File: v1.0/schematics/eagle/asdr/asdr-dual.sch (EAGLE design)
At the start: 56 parts, among them IC3 NE556, IC4 TL082P, Q1 2N3417, Q2 2N3417, Q3 2N3417, Q4 2N3417, Q5 2N3417, Q6 2N3417

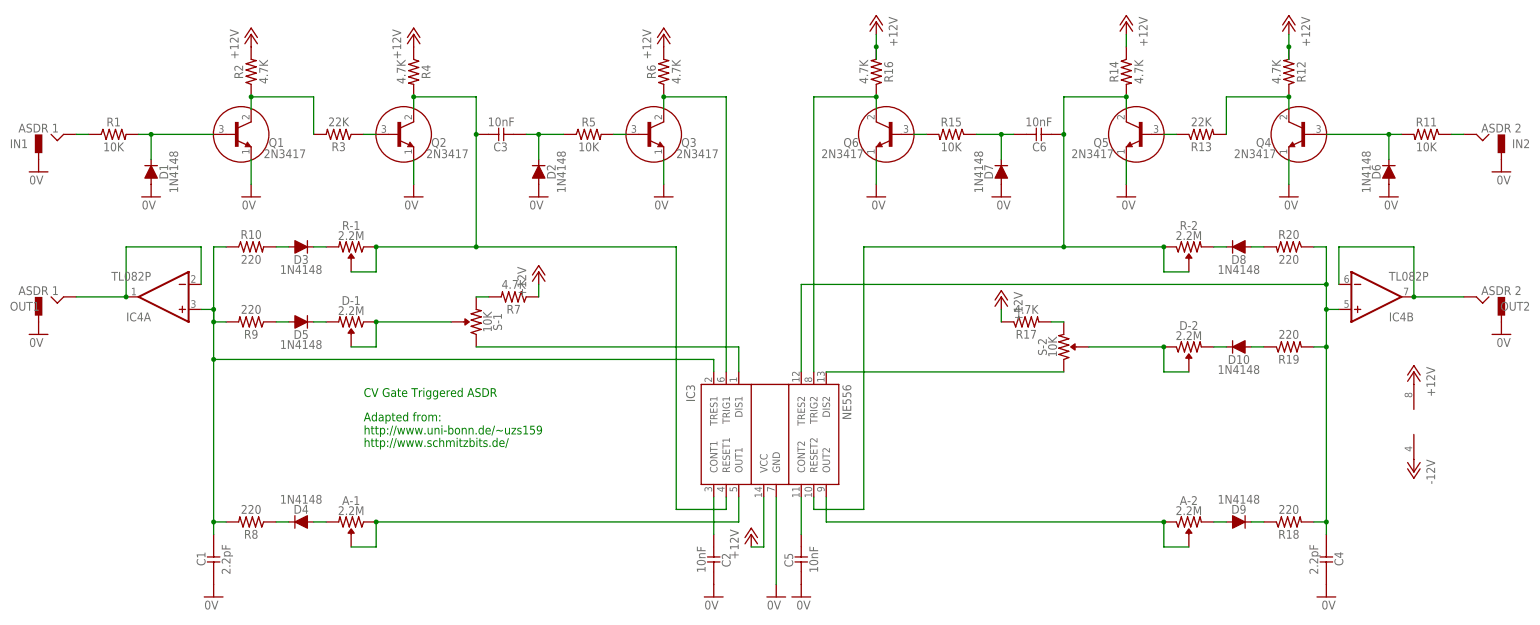
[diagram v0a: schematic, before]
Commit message: Updated ASDR with revised values
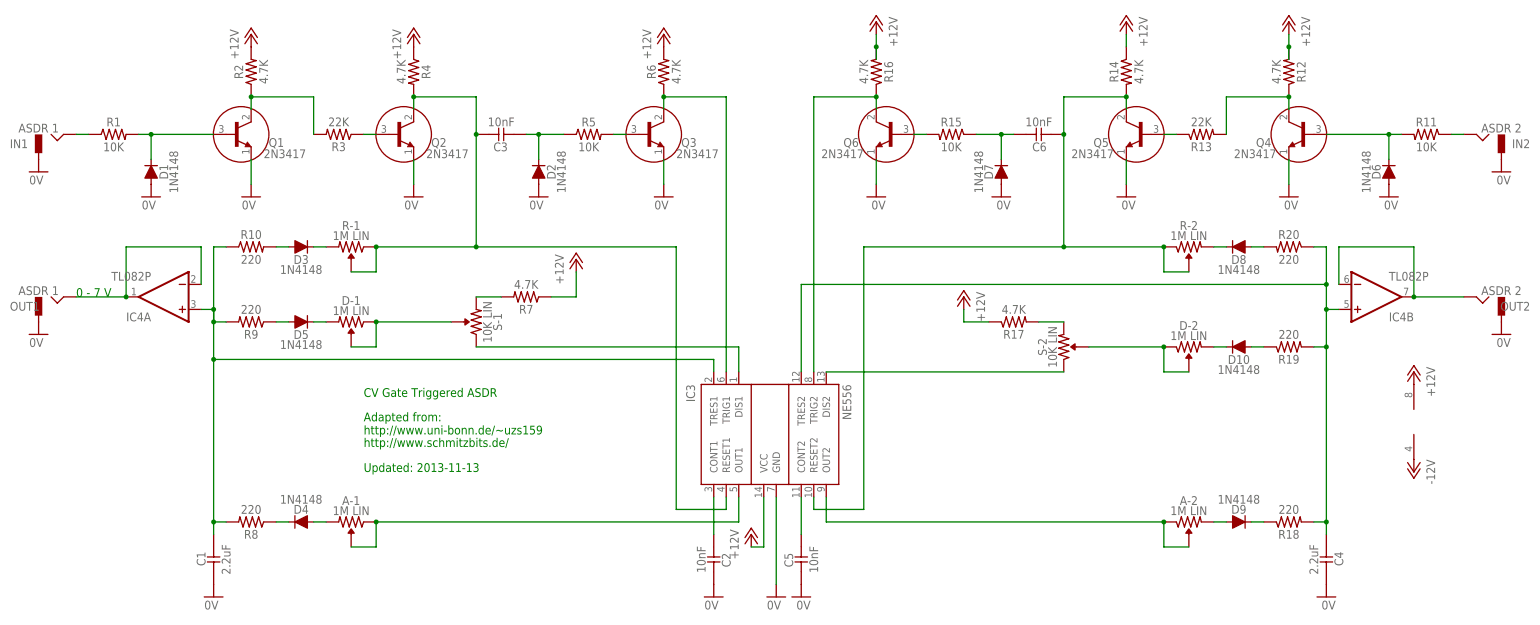
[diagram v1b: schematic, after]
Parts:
- A-1, A-2, D-1, D-2, R-1, R-2: value 2.2M -> 1M LIN
- C1, C4: value 2.2pF -> 2.2uF
- S-1, S-2: value 10K -> 10K LIN
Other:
- note added: "0 - 7 V"
- note added: "Updated: 2013-11-13"
- moved on the sheet: R17, R7
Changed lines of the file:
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@@
 <part name="R6" library="_common" deviceset="R" device="0309/10" value="4.7K"/>
 <part name="R7" library="_common" deviceset="R" device="0309/10" value="4.7K"/>
-<part name="S-1" library="_common" deviceset="R-VAR" device="" value="10K"/>
-<part name="D-1" library="_common" deviceset="R-VAR" device="" value="2.2M"/>
-<part name="A-1" library="_common" deviceset="R-VAR" device="" value="2.2M"/>
-<part name="R-1" library="_common" deviceset="R-VAR" device="" value="2.2M"/>
+<part name="S-1" library="_common" deviceset="R-VAR" device="" value="10K LIN"/>
+<part name="D-1" library="_common" deviceset="R-VAR" device="" value="1M LIN"/>
+<part name="A-1" library="_common" deviceset="R-VAR" device="" value="1M LIN"/>
+<part name="R-1" library="_common" deviceset="R-VAR" device="" value="1M LIN"/>
 <part name="R8" library="_common" deviceset="R" device="0309/10" value="220"/>
 <part name="R9" library="_common" deviceset="R" device="0309/10" value="220"/>
@@
 <part name="D5" library="_common" deviceset="1N4148" device=""/>
 <part name="R10" library="_common" deviceset="R" device="0309/10" value="220"/>
-<part name="C1" library="_common" deviceset="CC-US" device="025-024X044" value="2.2pF"/>
+<part name="C1" library="_common" deviceset="CC-US" device="025-024X044" value="2.2uF"/>
 <part name="C2" library="_common" deviceset="CC-US" device="025-024X044" value="10nF"/>
 <part name="C3" library="_common" deviceset="CC-US" device="025-024X044" value="10nF"/>
@@
 <part name="R16" library="_common" deviceset="R" device="0309/10" value="4.7K"/>
 <part name="R17" library="_common" deviceset="R" device="0309/10" value="4.7K"/>
-<part name="S-2" library="_common" deviceset="R-VAR" device="" value="10K"/>
-<part name="D-2" library="_common" deviceset="R-VAR" device="" value="2.2M"/>
-<part name="A-2" library="_common" deviceset="R-VAR" device="" value="2.2M"/>
-<part name="R-2" library="_common" deviceset="R-VAR" device="" value="2.2M"/>
+<part name="S-2" library="_common" deviceset="R-VAR" device="" value="10K LIN"/>
+<part name="D-2" library="_common" deviceset="R-VAR" device="" value="1M LIN"/>
+<part name="A-2" library="_common" deviceset="R-VAR" device="" value="1M LIN"/>
+<part name="R-2" library="_common" deviceset="R-VAR" device="" value="1M LIN"/>
 <part name="R18" library="_common" deviceset="R" device="0309/10" value="220"/>
 <part name="R19" library="_common" deviceset="R" device="0309/10" value="220"/>
@@
 <part name="D10" library="_common" deviceset="1N4148" device=""/>
 <part name="R20" library="_common" deviceset="R" device="0309/10" value="220"/>
-<part name="C4" library="_common" deviceset="CC-US" device="025-024X044" value="2.2pF"/>
+<part name="C4" library="_common" deviceset="CC-US" device="025-024X044" value="2.2uF"/>
 <part name="C5" library="_common" deviceset="CC-US" device="025-024X044" value="10nF"/>
 <part name="C6" library="_common" deviceset="CC-US" device="025-024X044" value="10nF"/>
@@
 http://www.uni-bonn.de/~uzs159</text>
 <text x="50.8" y="20.32" size="1.778" layer="91">http://www.schmitzbits.de/</text>
+<text x="50.8" y="15.24" size="1.778" layer="91">Updated: 2013-11-13</text>
+<text x="-7.62" y="50.8" size="1.778" layer="91">0 - 7 V</text>
 </plain>
 <instances>
@@
 <instance part="R5" gate="G$1" x="96.52" y="83.82"/>
 <instance part="R6" gate="G$1" x="111.76" y="96.52" rot="R90"/>
-<instance part="R7" gate="G$1" x="81.28" y="50.8" rot="R180"/>
+<instance part="R7" gate="G$1" x="83.82" y="50.8" rot="R180"/>
 <instance part="S-1" gate="G$1" x="73.66" y="45.72" rot="R90"/>
 <instance part="D-1" gate="G$1" x="48.26" y="45.72" rot="R180"/>
@@
 <instance part="P+2" gate="1" x="60.96" y="104.14"/>
 <instance part="P+3" gate="1" x="111.76" y="104.14"/>
-<instance part="P+5" gate="1" x="86.36" y="55.88"/>
+<instance part="P+5" gate="1" x="93.98" y="58.42"/>
 <instance part="GND1" gate="1" x="-15.24" y="76.2"/>
 <instance part="GND2" gate="1" x="-15.24" y="43.18"/>
@@
 <instance part="R15" gate="G$1" x="170.18" y="83.82" rot="MR0"/>
 <instance part="R16" gate="G$1" x="154.94" y="96.52" rot="MR90"/>
-<instance part="R17" gate="G$1" x="185.42" y="45.72" rot="MR180"/>
+<instance part="R17" gate="G$1" x="182.88" y="45.72" rot="MR180"/>
 <instance part="S-2" gate="G$1" x="193.04" y="40.64" rot="MR90"/>
 <instance part="D-2" gate="G$1" x="218.44" y="40.64" rot="MR180"/>
@@
 <instance part="P+8" gate="1" x="205.74" y="106.68" rot="MR0"/>
 <instance part="P+9" gate="1" x="154.94" y="106.68" rot="MR0"/>
-<instance part="P+10" gate="1" x="180.34" y="50.8" rot="MR0"/>
+<instance part="P+10" gate="1" x="172.72" y="50.8" rot="MR0"/>
 <instance part="GND11" gate="1" x="281.94" y="76.2" rot="MR0"/>
 <instance part="GND12" gate="1" x="281.94" y="43.18" rot="MR0"/>
@@
 <pinref part="R7" gate="G$1" pin="1"/>
 <pinref part="P+5" gate="1" pin="+12V"/>
-<wire x1="86.36" y1="50.8" x2="86.36" y2="53.34" width="0.1524" layer="91"/>
+<wire x1="88.9" y1="50.8" x2="93.98" y2="50.8" width="0.1524" layer="91"/>
+<wire x1="93.98" y1="50.8" x2="93.98" y2="55.88" width="0.1524" layer="91"/>
 </segment>
 <segment>
@@
 <pinref part="R17" gate="G$1" pin="1"/>
 <pinref part="P+10" gate="1" pin="+12V"/>
-<wire x1="180.34" y1="45.72" x2="180.34" y2="48.26" width="0.1524" layer="91"/>
+<wire x1="177.8" y1="45.72" x2="172.72" y2="45.72" width="0.1524" layer="91"/>
+<wire x1="172.72" y1="45.72" x2="172.72" y2="48.26" width="0.1524" layer="91"/>
 </segment>
 <segment>
@@
 <pinref part="R7" gate="G$1" pin="2"/>
 <pinref part="S-1" gate="G$1" pin="2"/>
-<wire x1="76.2" y1="50.8" x2="73.66" y2="50.8" width="0.1524" layer="91"/>
+<wire x1="78.74" y1="50.8" x2="73.66" y2="50.8" width="0.1524" layer="91"/>
 </segment>
 </net>
@@
 <pinref part="R17" gate="G$1" pin="2"/>
 <pinref part="S-2" gate="G$1" pin="2"/>
-<wire x1="190.5" y1="45.72" x2="193.04" y2="45.72" width="0.1524" layer="91"/>
-</segment>
-</net>
+<wire x1="187.96" y1="45.72" x2="193.04" y2="45.72" width="0.1524" layer="91"/>
+</segment>
+</net>

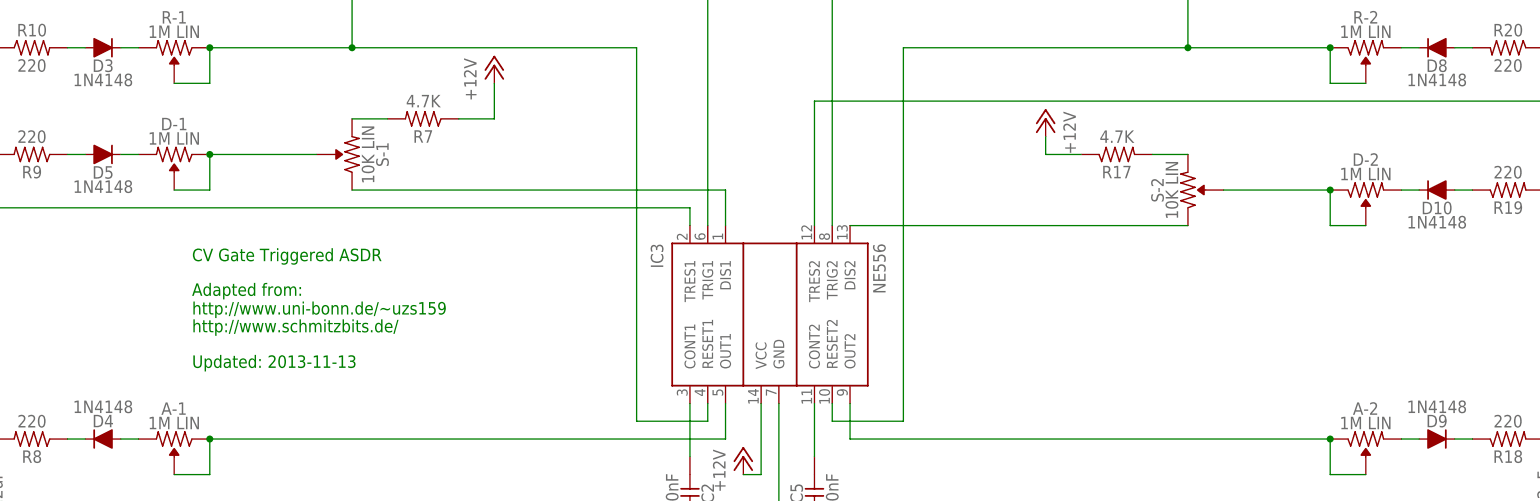
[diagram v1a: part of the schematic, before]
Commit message: Updated ASDR with 200K Log pots for decay
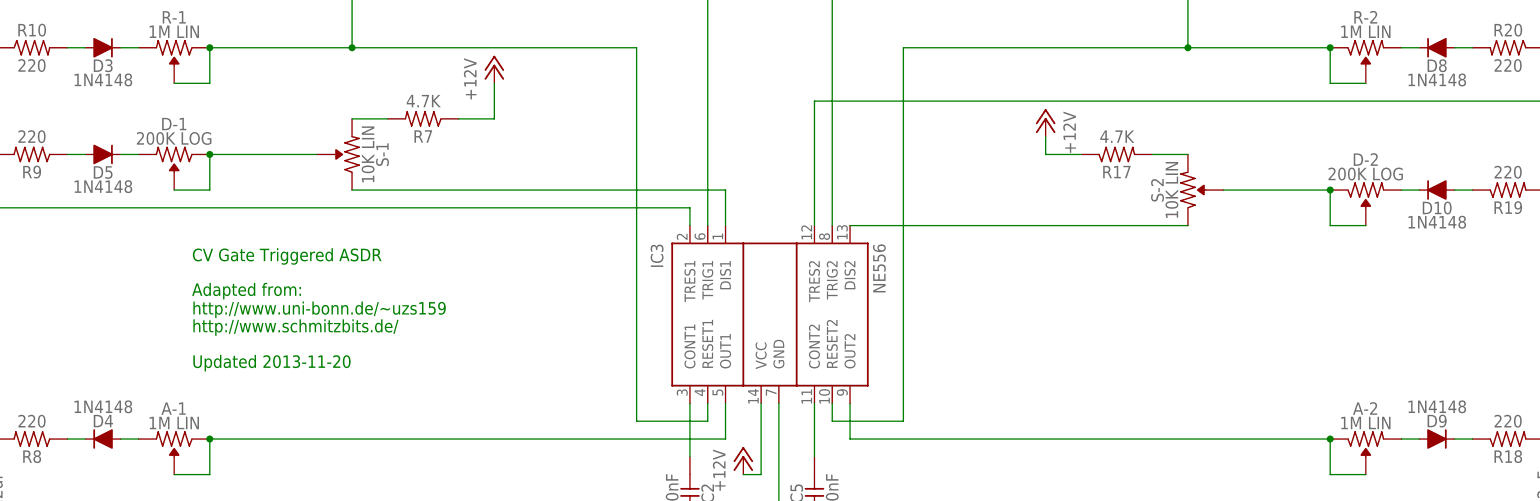
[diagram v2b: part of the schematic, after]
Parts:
- D-1, D-2: value 1M LIN -> 200K LOG
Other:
- note added: "Updated 2013-11-20"
- note removed: "Updated: 2013-11-13"
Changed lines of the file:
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@@
 <part name="R7" library="_common" deviceset="R" device="0309/10" value="4.7K"/>
 <part name="S-1" library="_common" deviceset="R-VAR" device="" value="10K LIN"/>
-<part name="D-1" library="_common" deviceset="R-VAR" device="" value="1M LIN"/>
+<part name="D-1" library="_common" deviceset="R-VAR" device="" value="200K LOG"/>
 <part name="A-1" library="_common" deviceset="R-VAR" device="" value="1M LIN"/>
 <part name="R-1" library="_common" deviceset="R-VAR" device="" value="1M LIN"/>
@@
 <part name="R17" library="_common" deviceset="R" device="0309/10" value="4.7K"/>
 <part name="S-2" library="_common" deviceset="R-VAR" device="" value="10K LIN"/>
-<part name="D-2" library="_common" deviceset="R-VAR" device="" value="1M LIN"/>
+<part name="D-2" library="_common" deviceset="R-VAR" device="" value="200K LOG"/>
 <part name="A-2" library="_common" deviceset="R-VAR" device="" value="1M LIN"/>
 <part name="R-2" library="_common" deviceset="R-VAR" device="" value="1M LIN"/>
@@
 http://www.uni-bonn.de/~uzs159</text>
 <text x="50.8" y="20.32" size="1.778" layer="91">http://www.schmitzbits.de/</text>
-<text x="50.8" y="15.24" size="1.778" layer="91">Updated: 2013-11-13</text>
 <text x="-7.62" y="50.8" size="1.778" layer="91">0 - 7 V</text>
+<text x="50.8" y="15.24" size="1.778" layer="91">Updated 2013-11-20</text>
 </plain>
 <instances>
